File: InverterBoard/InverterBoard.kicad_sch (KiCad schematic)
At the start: 2 parts, among them J1 to inverter PCB, U1 STGIPS10K60A

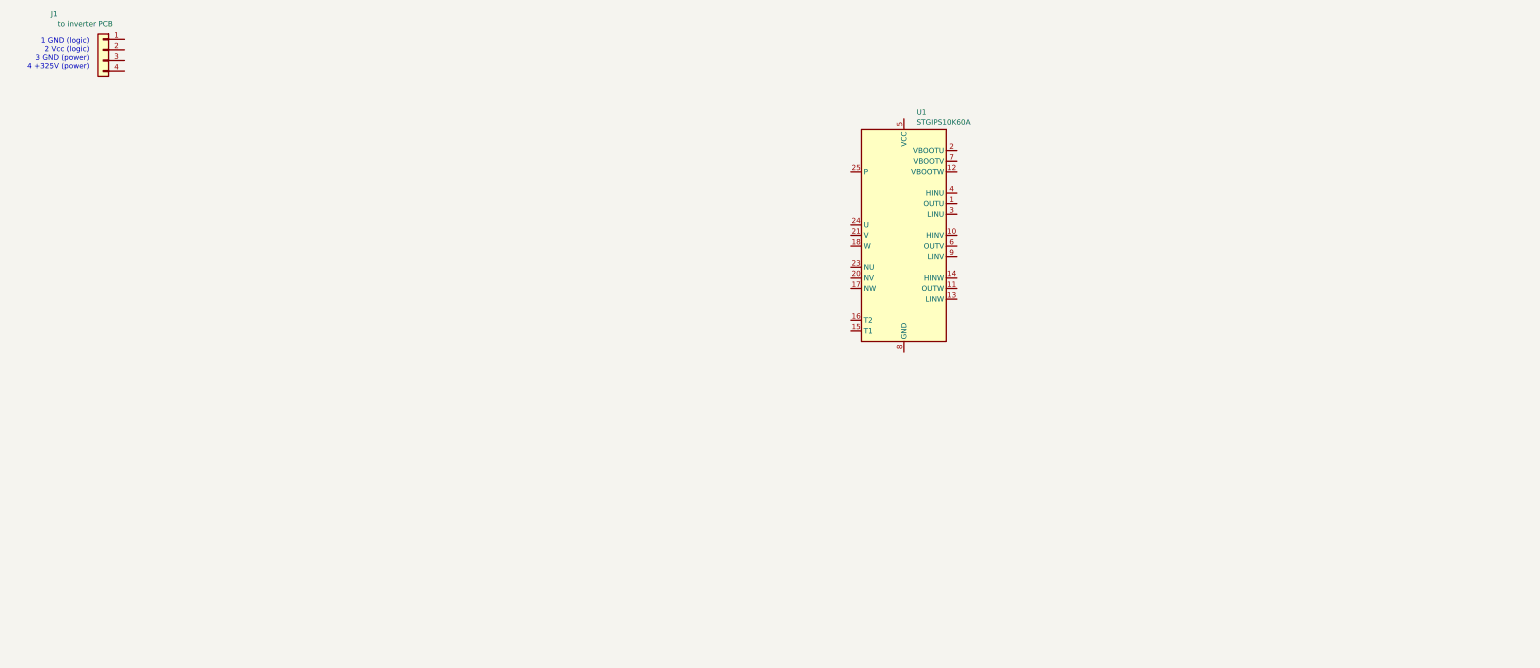
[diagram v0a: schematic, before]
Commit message: documenting high-power output stage
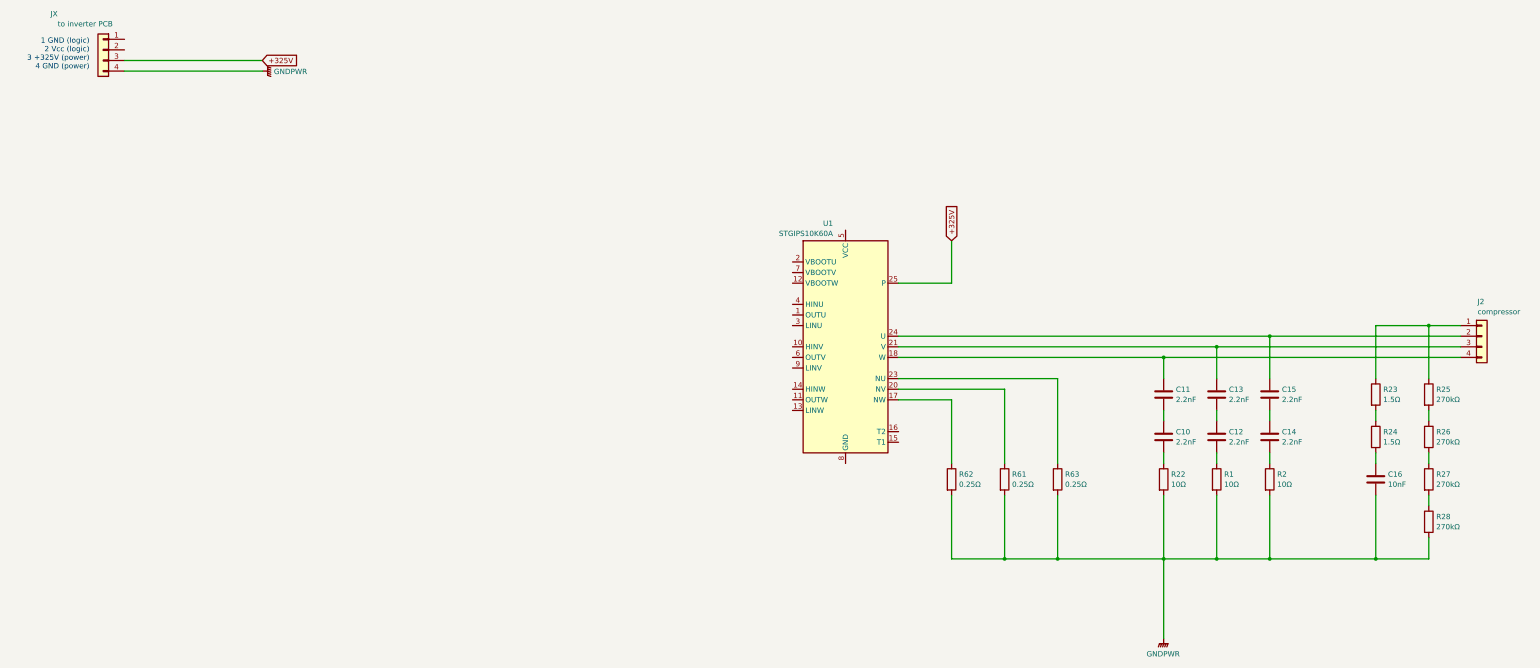
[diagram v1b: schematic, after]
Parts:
- added C10, C11, C12, C13, C14, C15: 2.2nF, Capacitor_SMD:C_1206_3216Metric, symbol Device:C
- added C16: 10nF, Capacitor_SMD:C_1206_3216Metric, symbol Device:C
- added J2: compressor, symbol Connector_Generic:Conn_01x04
- added R1, R2, R22: 10Ω, symbol Device:R
- added R23, R24: 1.5Ω, Resistor_SMD:R_1206_3216Metric, symbol Device:R
- added R25, R26, R27, R28: 270kΩ, Resistor_SMD:R_0805_2012Metric, symbol Device:R
- added R61, R62, R63: 0.25Ω, symbol Device:R
- renumbered J1 to JX
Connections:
- net at U1.17 (NW): now also R62.1
- net at U1.18 (W): now also C11.1, J2.4 (Pin_4)
- net +325V: now reaches U1.19 (P), U1.22 (P), U1.25 (P)
- net +325V: now also JX.3 (Pin_3)
- net at U1.20 (NV): now also R61.1
- net at U1.21 (V): now also C13.1, J2.3 (Pin_3)
- net at U1.23 (NU): now also R63.1
- net at U1.24 (U): now also C15.1, J2.2 (Pin_2)
- net GNDPWR: now reaches JX.4 (Pin_4)
- net GNDPWR: now also C16.2, R1.2, R2.2, R22.2, R28.2, R61.2, R62.2, R63.2
- new net: C14.1, C15.2
- new net: R26.2, R27.1
- new net: R27.2, R28.1
- new net: C12.2, R1.1
- new net: C10.2, R22.1
- new net: R25.2, R26.1
- new net: C14.2, R2.1
- new net: J2.1 (Pin_1), R23.1, R25.1
- new net: R23.2, R24.1
- new net: C10.1, C11.2
- new net: C12.1, C13.2
- new net: C16.1, R24.2
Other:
- note added: "1 GND (logic) 2 Vcc (logic) 3 +325V (power) 4 GND (power)"
- note removed: "1 GND (logic) 2 Vcc (logic) 3 GND (power) 4 +325V (power)"
- moved on the sheet: U1

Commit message: moving things around; fixing errors; begin documenting U6
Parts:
- added C1: 2.2nF, symbol Device:C
- added C2, C79: ??nF, Capacitor_SMD:C_0603_1608Metric, symbol Device:C
- added C51, C52, C53: ??nF, Capacitor_SMD:C_0805_2012Metric, symbol Device:C
- added R102, R103, R90, R91, R96, R97: 806Ω, symbol Device:R
- added R104, R3: 11.5kΩ ??, Resistor_SMD:R_0603_1608Metric, symbol Device:R
- added R4: 11.5kΩ, Resistor_SMD:R_0603_1608Metric, symbol Device:R
- added R94: 5.76kΩ, Resistor_SMD:R_0603_1608Metric, symbol Device:R
- added U2, U6: TSH24, symbol Amplifier_Operational:LMC6484
- R61: symbol Device:R -> Device:R_Shunt
- R62: renamed from R63; symbol Device:R -> Device:R_Shunt
- R63: renamed from R62; symbol Device:R -> Device:R_Shunt
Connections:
- net at J2.2 (Pin_2), U1.24 (U): now also C11.1; no longer C15.1
- net at U1.1 (OUTU): now also C53.2
- net at U1.11 (OUTW): now also C51.2
- net at U1.12 (VBOOTW): now also C51.1
- net at J2.4 (Pin_4), U1.18 (W): now also C15.1; no longer C11.1
- net at U1.2 (VBOOTU): now also C53.1
- net VCC: now reaches U1.5 (VCC)
- net VCC: now also JX.2 (Pin_2), U2.4 (V+)
- net at U1.6 (OUTV): now also C52.2
- net at U1.7 (VBOOTV): now also C52.1
- net GND: now reaches U1.8 (GND)
- net GND: now also C16.2, JX.4 (Pin_4), R1.2, R2.2, R22.2, R28.2, R61.4, R62.4, R63.4, C2.1, R4.2, U2.11 (V-)
- removed net GNDPWR: C16.2, JX.4 (Pin_4), R1.2, R2.2, R22.2, R28.2, R61.2, R62.2, R63.2
- new net: R102.1, R62.2
- new net: C79.1, R94.2, U6.1
- new net: C79.2, R90.2, R94.1, U6.2 (-)
- new net: C2.2, R4.1, R91.2, U6.3 (+)
- new net: R63.2, R97.1
- new net: R63.3, R96.1
- new net: R103.1, R62.3
- new net: C1.2, R103.2, U2.5 (+)
- new net: R61.3, R90.1
- new net: R61.2, R91.1
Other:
- note added: "1 ?? 2 Vcc (OPA, IPM, ??) 3 +325V 4 GND"
- note added: "Pin3 OPV"
- note removed: "1 GND (logic) 2 Vcc (logic) 3 +325V (power) 4 GND (power)"
- moved on the sheet: C12, C13, C14, C15, C16, J2, R1, R2, R23, R24, R25, R26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

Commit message: moving around stuff
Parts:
- C1: value 2.2nF -> ??nF
- R61, R62, R63: value 0.25Ω -> 25mΩ
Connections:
- net at C1.2, U2.5 (+): no longer R103.2
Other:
- note removed: "Pin3 OPV"
- moved on the sheet: C1, C10, C11, C12, C13, C14, C15, C16, C2, C51, C52, C53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
